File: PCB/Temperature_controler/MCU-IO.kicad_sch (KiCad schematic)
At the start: 14 parts, among them U1 STM32F401RBTx

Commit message: PCB progress
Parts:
- removed C7: 100nF, symbol Device:C
- added C21, C22, C23, C24: 18pF, Capacitor_SMD:C_0805_2012Metric_Pad1.18x1.45mm_HandSolder, symbol Device:C
- added C25: 100nF, Capacitor_SMD:C_0805_2012Metric_Pad1.18x1.45mm_HandSolder, symbol Device:C
- added J3: Conn_02x03, Connector_RJ:RJ45_Amphenol_RJHSE538X, symbol Connector_Generic:Conn_02x03_Counter_Clockwise
- added R7: 5,1kΩ, Resistor_SMD:R_0805_2012Metric_Pad1.20x1.40mm_HandSolder, symbol Device:R
- added SW2: SW_Push, Button_Switch_SMD:SW_Push_1P1T-SH_NO_CK_KMR2xxG, symbol Switch:SW_Push
- added XTAL1: NX2016SA-32M-EXS00A-CS06465, NX2016SA-32M-EXS00A-CS06465:NX2016SA_NDK, symbol NX2016SA-32M-EXS00A-CS06465:NX2016SA-32M-EXS00A-CS06465
- added Y1: NX2012SA-32.768K-STD-MUB-1, NX2012SA-32.768K-STD-MUB-1:XTAL_NX2012SA-32.768K-STD-MUB-1, symbol NX2012SA-32.768K-STD-MUB-1:NX2012SA-32.768K-STD-MUB-1
- C1, C10, C11, C12, C2, C3, C4, C5, C6, C8, C9: footprint (none) -> Capacitor_SMD:C_0805_2012Metric_Pad1.18x1.45mm_HandSolder
- FB1: footprint (none) -> Fuse:Fuse_2010_5025Metric_Pad1.52x2.65mm_HandSolder
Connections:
- net +3.3V: now also J3.6 (Pin_6), SW2.1
- net GND: now also C21.2, C22.2, C23.2, C24.2, C25.1, J3.3 (Pin_3), R7.1, XTAL1.2, XTAL1.4
- net LSE_IN: now also C21.1, Y1.2
- net LSE_OUT: now also C22.1, Y1.1
- net RS485_DIR: now reaches U1.15 (PA1)
- net RS485_Tx: now reaches U1.16 (PA2)
- net RS485_RX: now reaches U1.17 (PA3)
- net RTD1_CS: now reaches U1.20 (PA4)
- net TC1_FAULT: now reaches U1.25 (PC5)
- net RTD2_CS: now reaches U1.26 (PB0)
- net RTD2_DRDY: now reaches U1.27 (PB1)
- net RTD1_DRDY: now reaches U1.28 (PB2)
- net SSR1: now reaches U1.33 (PB12)
- net SSR2: now reaches U1.34 (PB13)
- net SSR3: now reaches U1.35 (PB14)
- net SSR4: now reaches U1.36 (PB15)
- net TC1_DRDY: now reaches U1.37 (PC6)
- net TC2_CS: now reaches U1.38 (PC7)
- net TC2_FAULT: now reaches U1.39 (PC8)
- net TC2_DRDY: now reaches U1.40 (PC9)
- net SWDIO: now reaches U1.46 (PA13)
- net SWDIO: now also J3.5 (Pin_5)
- net SWCLK: now reaches U1.49 (PA14)
- net SWCLK: now also J3.2 (Pin_2)
- net HSE_IN: now reaches U1.5 (PH0)
- net HSE_IN: now also C24.1, XTAL1.1
- net SWO: now reaches U1.55 (PB3)
- net SWO: now also J3.4 (Pin_4)
- net HSE_OUT: now reaches U1.6 (PH1)
- net HSE_OUT: now also C23.1, XTAL1.3
- net BOOT: now reaches U1.60 (BOOT0)
- net BOOT: now also R7.2, SW2.2
- net NRST: now reaches U1.7 (NRST)
- net NRST: now also C25.2, J3.1 (Pin_1)
- net MAX31856_CS: no longer names the net of U1.10 (PC2)
- net MAX31856_DRDY renamed TC1_CS
- net MAX31856_FAULT: no longer names the net of U1.11 (PC3)
- net MAX31865_CS: no longer names the net of U1.9 (PC1)
- net MAX31865_DRDY: no longer names the net of U1.8 (PC0)
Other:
- note added: "Boot"
- note added: "HSE Oscillator"
- note added: "LSE Oscillator"
- note added: "STM32 MCU"
- note added: "SWD Connector"
- note removed: "Oscillators"
- moved on the sheet: C1, C10, C11, C12, C2, C3, C4, C5, C6, C8, C9, FB1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

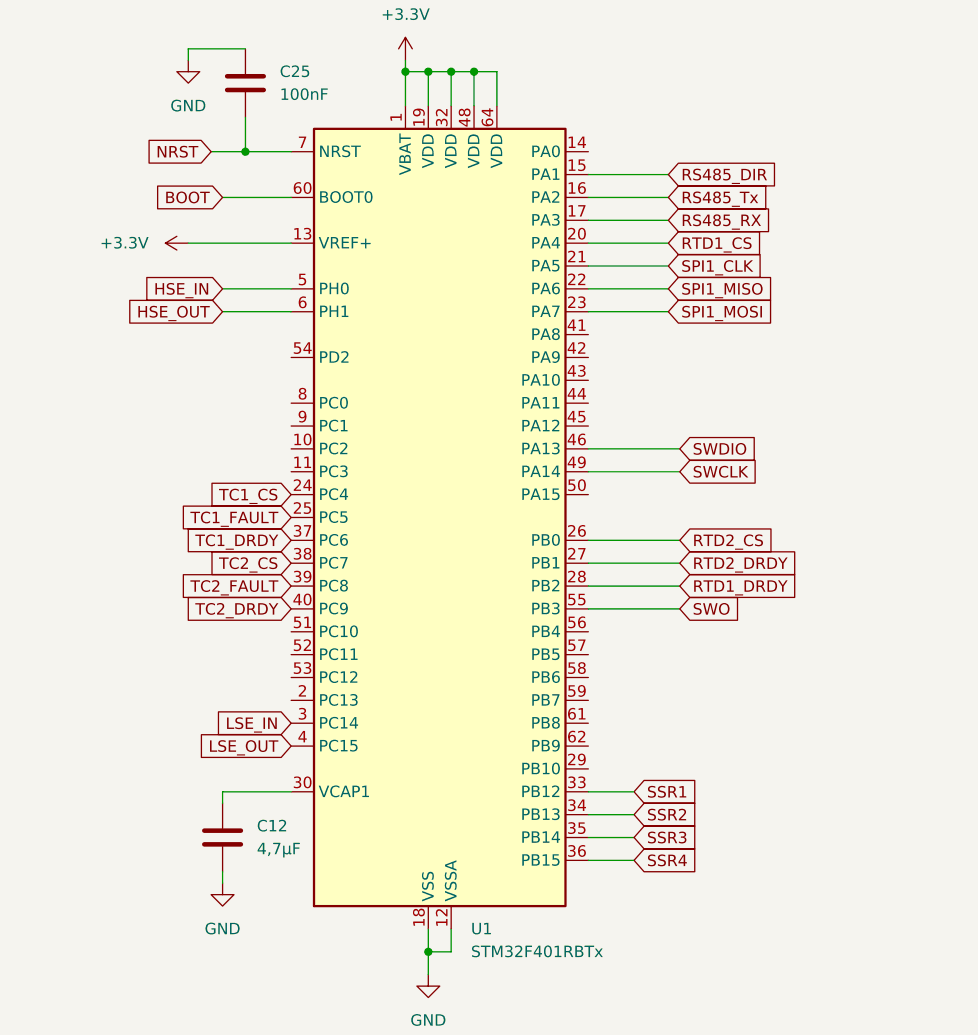
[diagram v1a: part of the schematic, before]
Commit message: Schematic update, PCB progress
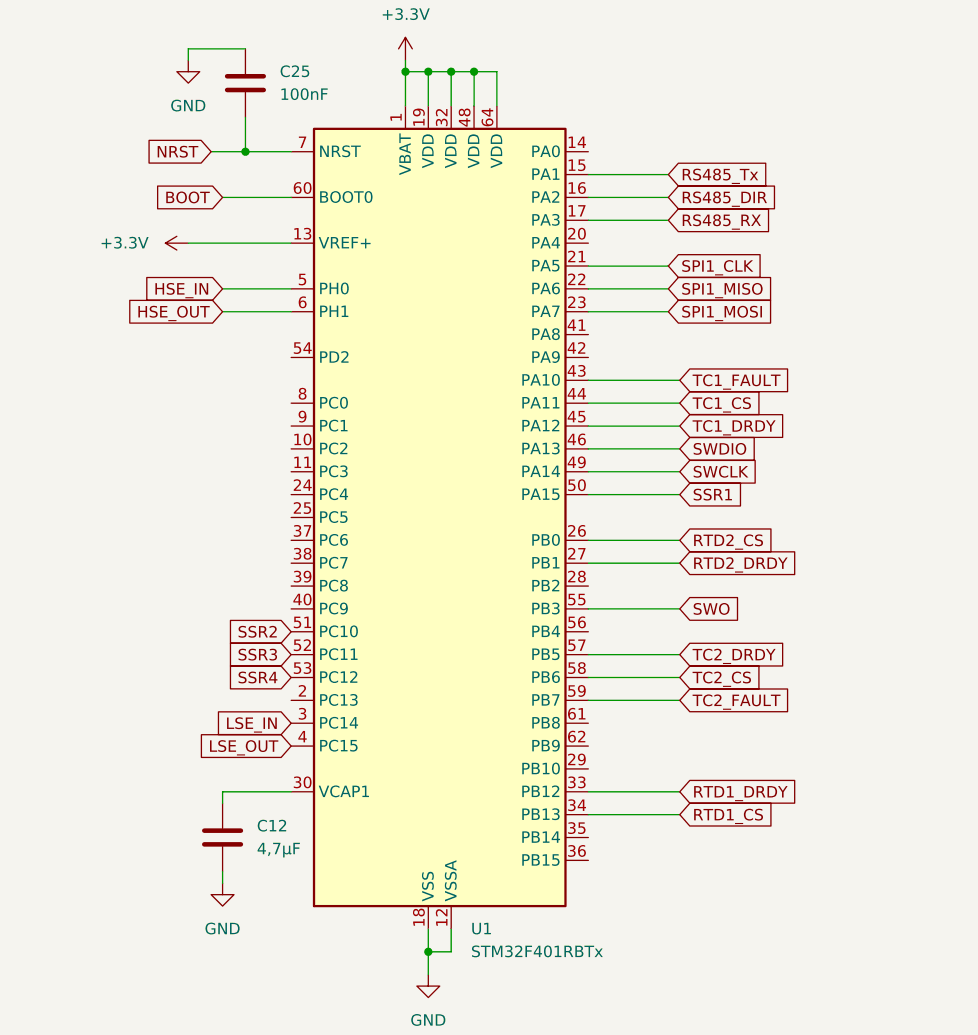
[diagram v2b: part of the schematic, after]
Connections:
- net RS485_DIR: now also U1.16 (PA2); no longer U1.15 (PA1)
- net RS485_Tx: now also U1.15 (PA1); no longer U1.16 (PA2)
- net RTD1_CS: now also U1.34 (PB13); no longer U1.20 (PA4)
- net RTD1_DRDY: now also U1.33 (PB12); no longer U1.28 (PB2)
- net SSR1: now also U1.50 (PA15); no longer U1.33 (PB12)
- net SSR2: now also U1.51 (PC10); no longer U1.34 (PB13)
- net SSR3: now also U1.52 (PC11); no longer U1.35 (PB14)
- net SSR4: now also U1.53 (PC12); no longer U1.36 (PB15)
- net TC1_CS: now also U1.44 (PA11); no longer U1.24 (PC4)
- net TC1_DRDY: now also U1.45 (PA12); no longer U1.37 (PC6)
- net TC1_FAULT: now also U1.43 (PA10); no longer U1.25 (PC5)
- net TC2_CS: now also U1.58 (PB6); no longer U1.38 (PC7)
- net TC2_DRDY: now also U1.57 (PB5); no longer U1.40 (PC9)
- net TC2_FAULT: now also U1.59 (PB7); no longer U1.39 (PC8)

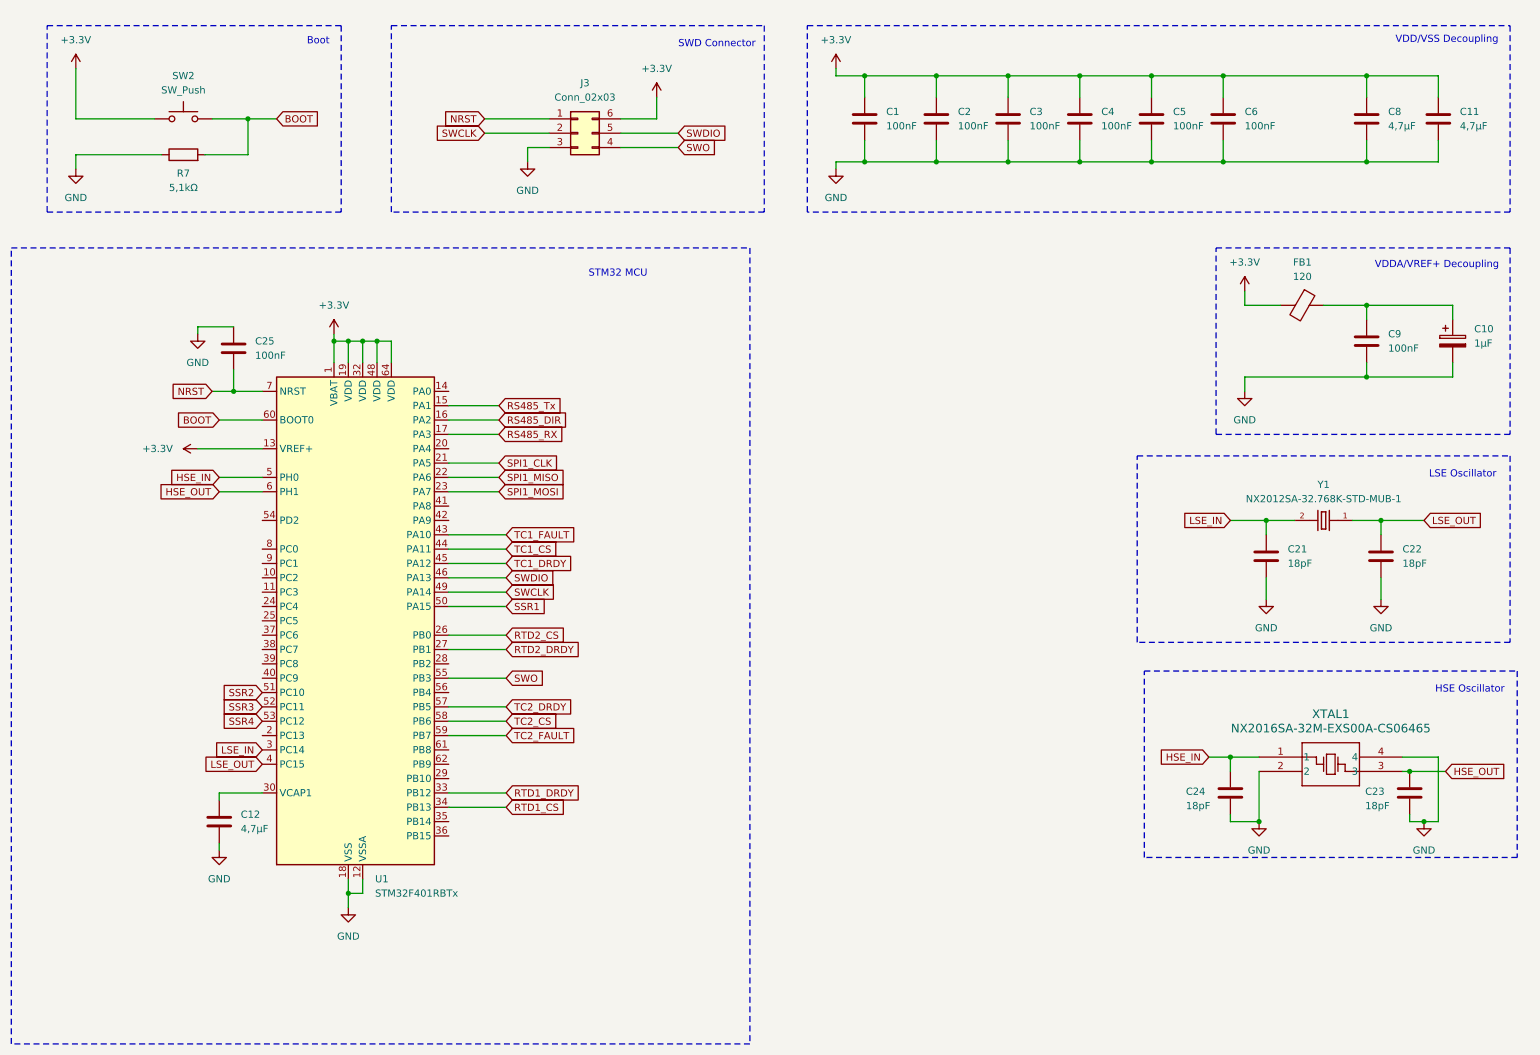
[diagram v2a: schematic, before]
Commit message: PCB traces changed
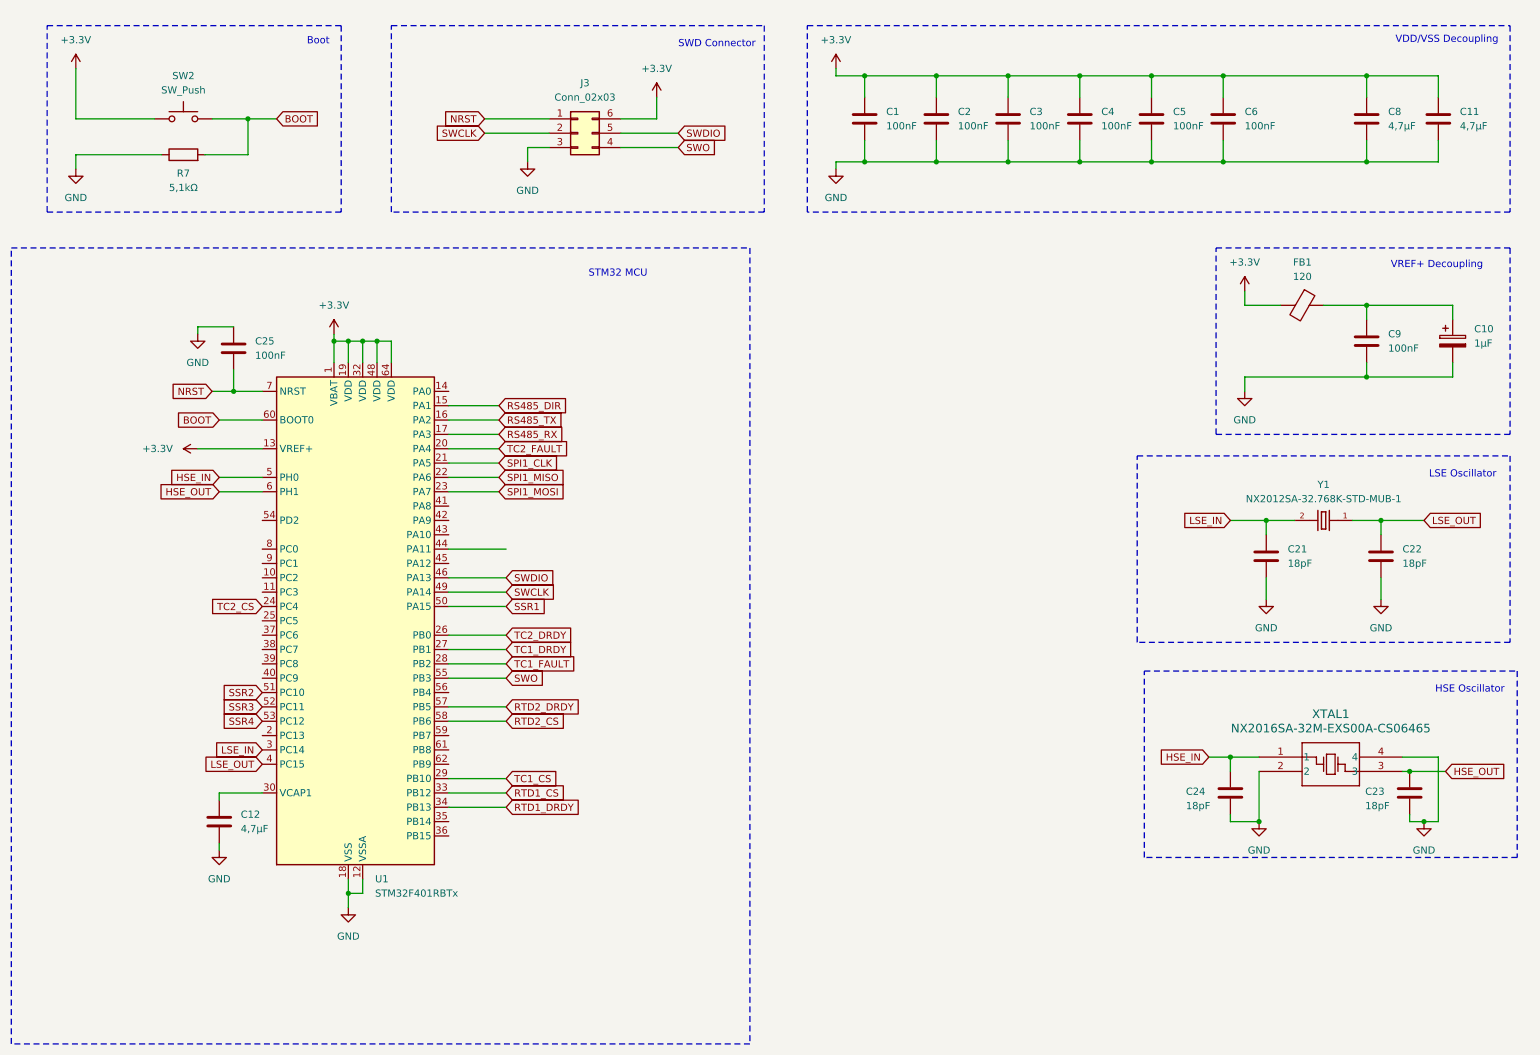
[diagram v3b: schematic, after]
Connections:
- net RS485_Tx is gone; now on net RS485_DIR: U1.15 (PA1)
- net RS485_DIR: no longer U1.16 (PA2)
- net RTD1_CS: now also U1.33 (PB12); no longer U1.34 (PB13)
- net RTD1_DRDY: now also U1.34 (PB13); no longer U1.33 (PB12)
- net RTD2_CS: now also U1.58 (PB6); no longer U1.26 (PB0)
- net RTD2_DRDY: now also U1.57 (PB5); no longer U1.27 (PB1)
- net TC1_CS: now also U1.29 (PB10); no longer U1.44 (PA11)
- net TC1_DRDY: now also U1.27 (PB1); no longer U1.45 (PA12)
- net TC1_FAULT: now also U1.28 (PB2); no longer U1.43 (PA10)
- net TC2_CS: now also U1.24 (PC4); no longer U1.58 (PB6)
- net TC2_DRDY: now also U1.26 (PB0); no longer U1.57 (PB5)
- net TC2_FAULT: now also U1.20 (PA4); no longer U1.59 (PB7)
- new net RS485_TX: U1.16 (PA2)
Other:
- note added: "VREF+ Decoupling"
- note removed: "VDDA/VREF+ Decoupling"

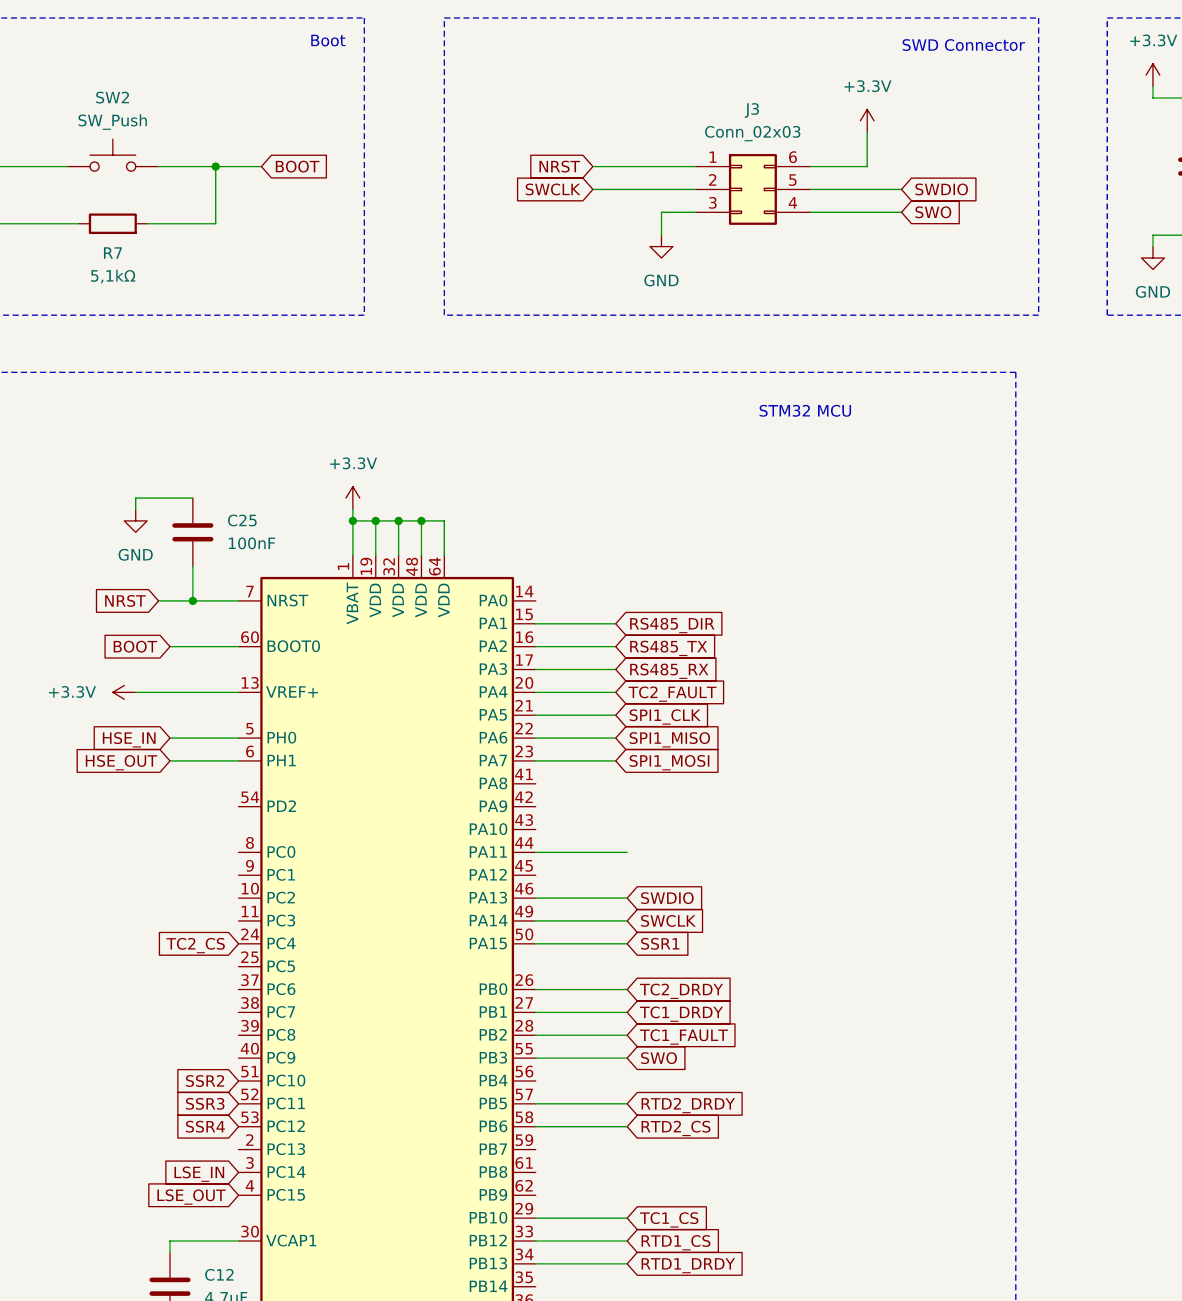
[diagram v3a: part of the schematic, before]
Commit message: PCB update and sensor abstraction layer
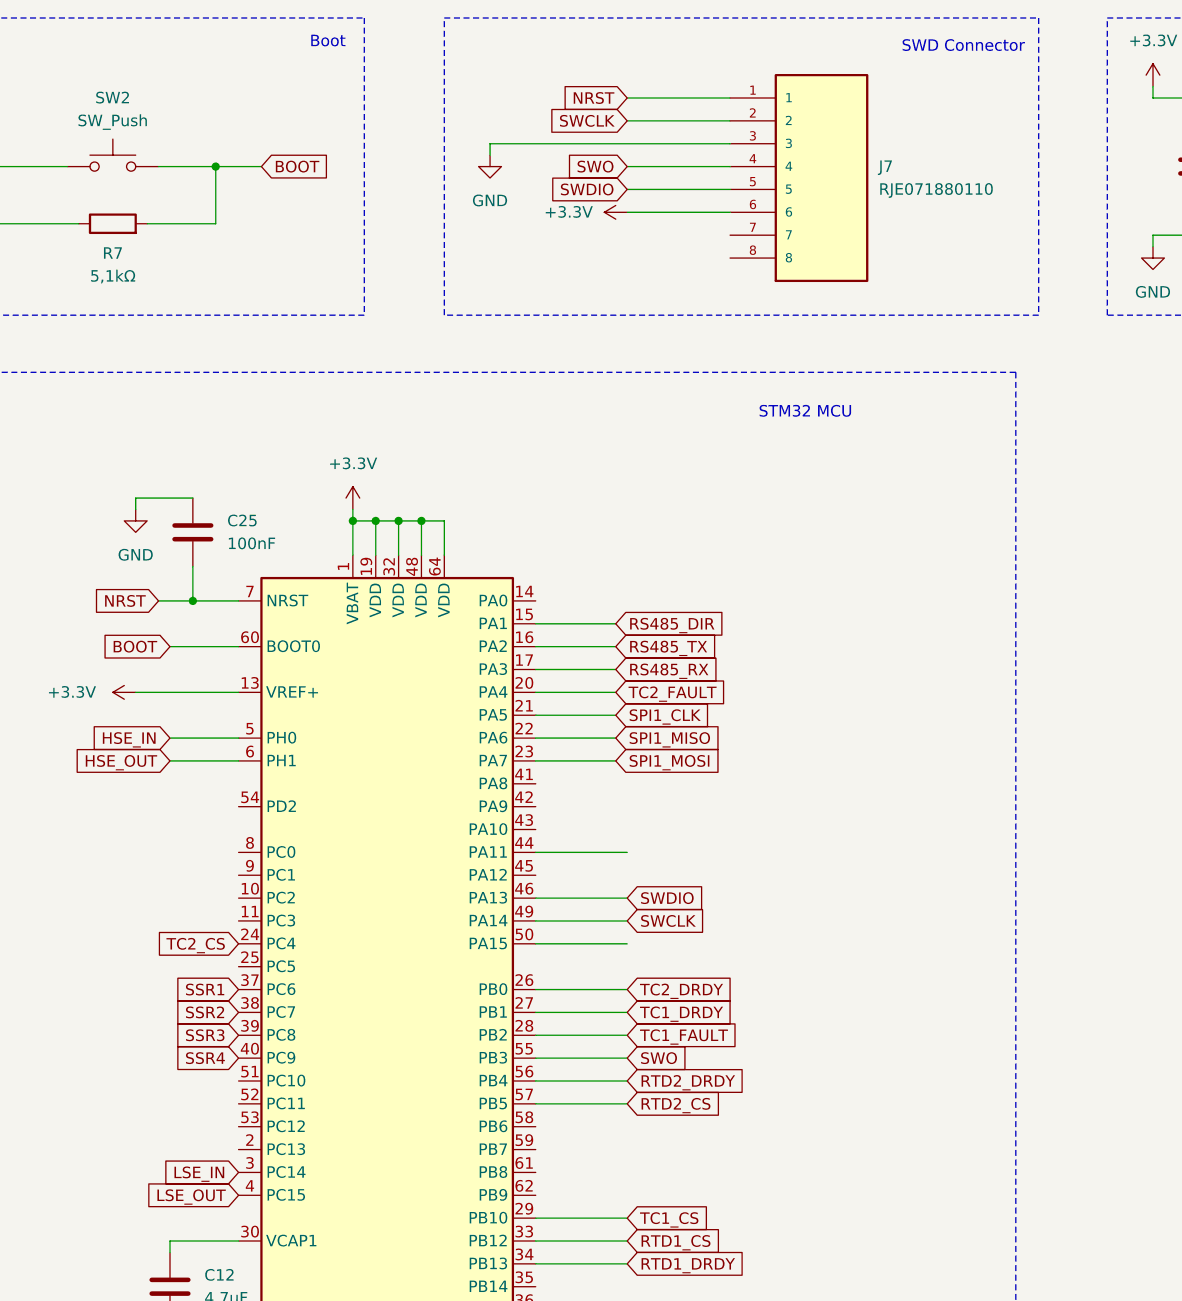
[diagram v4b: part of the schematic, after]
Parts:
- removed J3: Conn_02x03, Connector_RJ:RJ45_Amphenol_RJHSE538X, symbol Connector_Generic:Conn_02x03_Counter_Clockwise
- added J7: RJE071880110, RJE071880110:AMPHENOL_RJE071880110, symbol RJE071880110:RJE071880110
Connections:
- net +3.3V: now also J7.6
- net GND: now also J7.3
- net NRST: now also J7.1
- net RTD2_CS: now also U1.57 (PB5); no longer U1.58 (PB6)
- net RTD2_DRDY: now also U1.56 (PB4); no longer U1.57 (PB5)
- net SSR1: now also U1.37 (PC6); no longer U1.50 (PA15)
- net SSR2: now also U1.38 (PC7); no longer U1.51 (PC10)
- net SSR3: now also U1.39 (PC8); no longer U1.52 (PC11)
- net SSR4: now also U1.40 (PC9); no longer U1.53 (PC12)
- net SWCLK: now also J7.2
- net SWDIO: now also J7.5
- net SWO: now also J7.4
